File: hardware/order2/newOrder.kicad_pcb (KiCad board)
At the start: 2 copper layers, 200.1 x 330 mm, 683 parts, among them IC1 ATMEGA88-A, IC1 ATMEGA88A-A, J1 RJ45, J1 RJ45_8P8C_8FACH, K1 CONN_3, K1 pow_sel, K2 CONN_3, P1 CONN_4, P1 ISP, P1 UART, P2 CONN_4, P2 Shield, P2 UART, P2 so8, P3 CONN_4, P3 i2c_pow, P4 i2c_chain, P5 12Vin, P6 HOHLBUCHSE, P7 Vccin, P8 ISP, P9 5Vin, SW1 SW1, SW1 SW_RESET, SW2 SCHALTER_2POL, SW3 SW_RESET, U1 LM7805, U1 ST485, U1 TSIC50XF, U2 HYT271, U2 ST485, U3 ST485, U4 ST485, U5 ST485, U6 ST485, U7 ST485, U8 ST485, U9 ST485, X1 20MHz, m3_loch VAL**

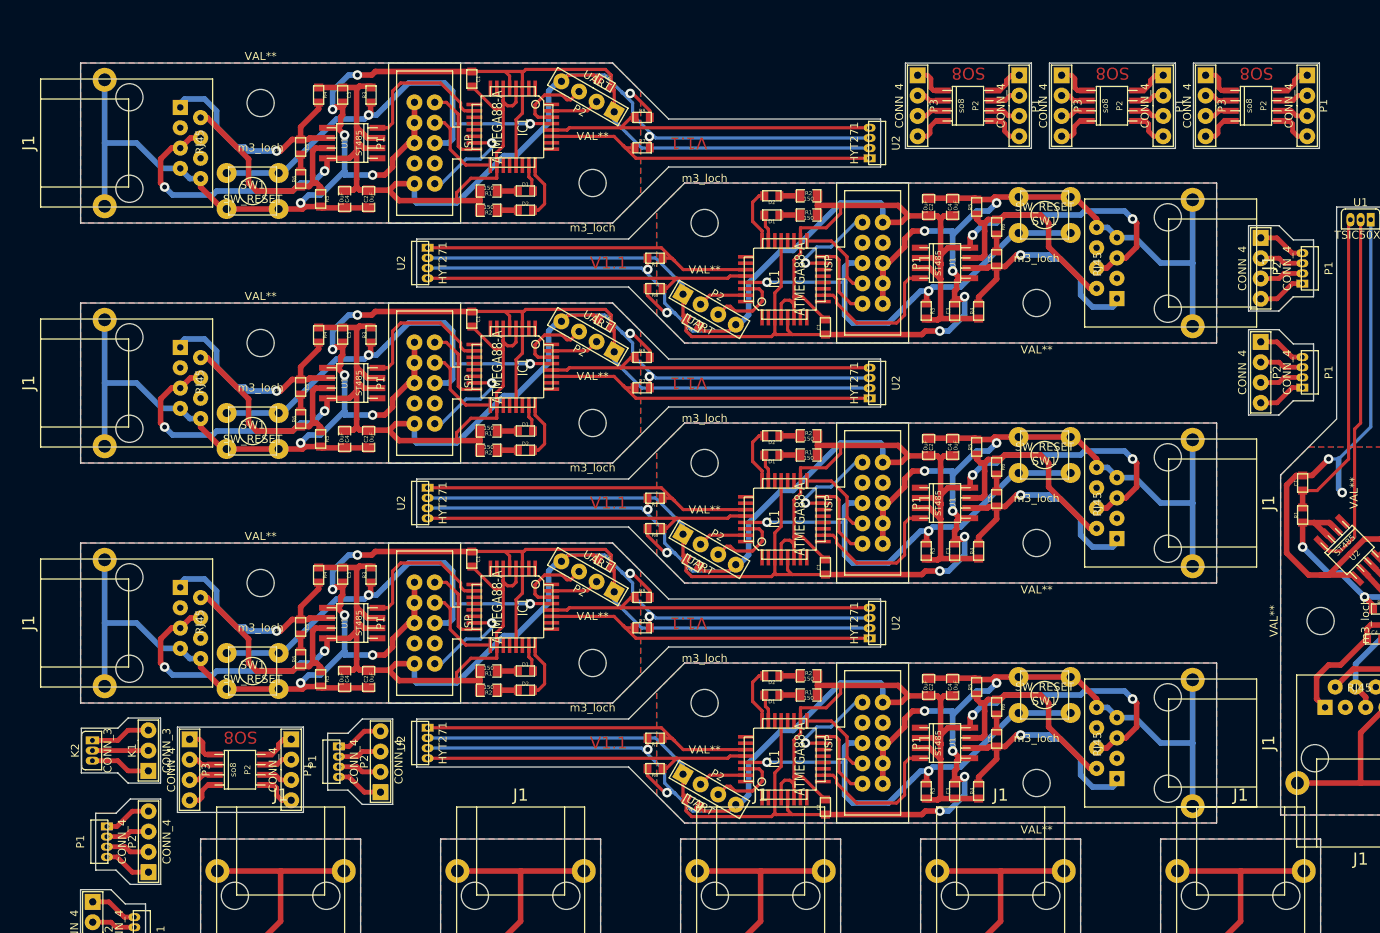
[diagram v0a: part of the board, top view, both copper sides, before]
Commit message: delete humility boards
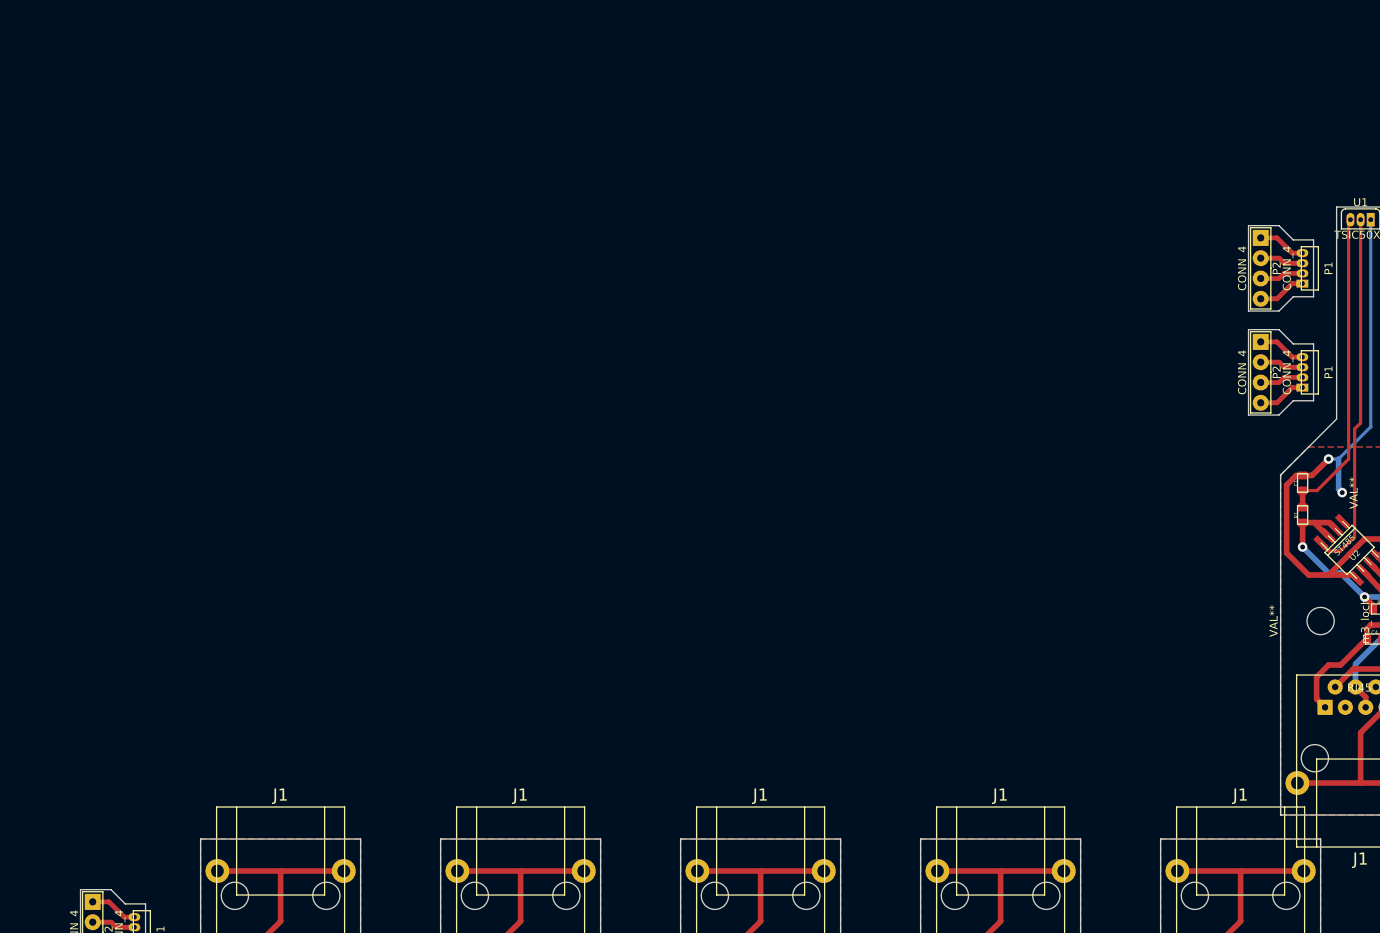
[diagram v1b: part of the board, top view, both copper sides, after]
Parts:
- removed the C1 at (68.9, 82.0)
- removed the C1 at (68.9, 22.0)
- removed the C1 at (113.1, 113.0)
- removed the C1 at (113.1, 53.0)
- removed the C1 at (113.1, 83.0)
- removed the C1 at (68.9, 52.0)
- removed the C2 at (56.0, 97.0)
- removed the C2 at (56.0, 37.0)
- removed the C2 at (126.0, 98.0)
- removed the C2 at (126.0, 38.0)
- removed the C2 at (126.0, 68.0)
- removed the C2 at (56.0, 67.0)
- removed the C3 at (52.8, 84.0)
- removed the C3 at (52.8, 24.0)
- removed the C3 at (129.2, 111.0)
- removed the C3 at (129.2, 51.0)
- removed the C3 at (129.2, 81.0)
- removed the C3 at (52.8, 54.0)
- removed the C4 at (53.0, 97.0)
- removed the C4 at (53.0, 37.0)
- removed the C4 at (129.0, 98.0)
- removed the C4 at (129.0, 38.0)
- removed the C4 at (129.0, 68.0)
- removed the C4 at (53.0, 67.0)
- removed the C5 at (47.5, 90.5)
- removed the C5 at (47.5, 30.5)
- removed the C5 at (134.5, 44.5)
- removed the C5 at (134.5, 74.5)
- removed the C5 at (47.5, 60.5)
- removed the C5 at (134.5, 104.5)
- removed the C6 at (85.5, 82.5)
- removed the C6 at (85.5, 22.5)
- removed the C6 at (96.5, 52.5)
- removed the C6 at (96.5, 82.5)
- removed the C6 at (85.5, 52.5)
- removed the C6 at (96.5, 112.5)
- removed the D1 at (75.6, 96.0)
- removed the D1 at (75.6, 36.0)
- removed the D1 at (106.4, 39.0)
- removed the D1 at (106.4, 69.0)
- removed the D1 at (75.6, 66.0)
- removed the D1 at (106.4, 99.0)
- removed the D2 at (75.6, 98.4)
- removed the D2 at (75.6, 38.4)
- removed the D2 at (106.4, 36.6)
- removed the D2 at (106.4, 66.6)
- removed the D2 at (75.6, 68.4)
- removed the D2 at (106.4, 96.6)
- removed the IC1 at (74.0, 88.0)
- removed the IC1 at (74.0, 28.0)
- removed the IC1 at (108.0, 47.0)
- removed the IC1 at (108.0, 77.0)
- removed the IC1 at (74.0, 58.0)
- removed the IC1 at (108.0, 107.0)
- removed the J1 at (35.0, 90.0)
- removed the J1 at (35.0, 30.0)
- removed the J1 at (147.0, 105.0)
- removed the J1 at (147.0, 45.0)
- removed the J1 at (147.0, 75.0)
- removed the J1 at (35.0, 60.0)
- removed the K1 at (28.5, 105.9)
- removed K2: CONN_3, Tsic_TO92
- removed the P1 at (63.0, 90.0)
- removed the P1 at (63.0, 30.0)
- removed the P1 at (119.0, 45.0)
- removed the P1 at (119.0, 75.0)
- removed the P1 at (63.0, 60.0)
- removed the P1 at (173.3, 25.3)
- removed the P1 at (23.4, 117.3)
- removed the P1 at (119.0, 105.0)
- removed the P1 at (155.3, 25.3)
- removed the P1 at (137.3, 25.3)
- removed the P1 at (46.3, 108.3)
- removed the P1 at (52.4, 107.3)
- removed the P2 at (83.4, 84.2)
- removed the P2 at (83.4, 24.2)
- removed the P2 at (98.6, 50.8)
- removed the P2 at (98.6, 80.8)
- removed the P2 at (83.4, 54.2)
- removed the P2 at (168.9, 25.3)
- removed the P2 at (28.5, 117.3)
- removed the P2 at (98.6, 110.8)
- removed the P2 at (150.9, 25.3)
- removed the P2 at (132.9, 25.3)
- removed the P2 at (41.9, 108.3)
- removed the P2 at (57.5, 107.3)
- removed the P3 at (142.6, 25.3)
- removed the P3 at (124.6, 25.3)
- removed the P3 at (33.6, 108.3)
- removed the P3 at (160.6, 25.3)
- removed the R1 at (71.0, 96.0)
- removed the R1 at (71.0, 36.0)
- removed the R1 at (111.0, 99.0)
- removed the R1 at (111.0, 39.0)
- removed the R1 at (111.0, 69.0)
- removed the R1 at (71.0, 66.0)
- removed the R2 at (71.0, 98.4)
- removed the R2 at (71.0, 38.4)
- removed the R2 at (111.0, 96.6)
- removed the R2 at (111.0, 36.6)
- removed the R2 at (111.0, 66.6)
- removed the R2 at (71.0, 68.4)
- removed the R3 at (56.3, 84.0)
- removed the R3 at (56.3, 24.0)
- removed the R3 at (125.7, 111.0)
- removed the R3 at (125.7, 51.0)
- removed the R3 at (125.7, 81.0)
- removed the R3 at (56.3, 54.0)
- removed the R4 at (49.8, 84.0)
- removed the R4 at (49.8, 24.0)
- removed the R4 at (132.2, 111.0)
- removed the R4 at (132.2, 51.0)
- removed the R4 at (132.2, 81.0)
- removed the R4 at (49.8, 54.0)
- removed the R5 at (50.0, 97.0)
- removed the R5 at (50.0, 37.0)
- removed the R5 at (132.0, 38.0)
- removed the R5 at (132.0, 68.0)
- removed the R5 at (50.0, 67.0)
- removed the R5 at (132.0, 98.0)
- removed the R6 at (47.5, 94.5)
- removed the R6 at (47.5, 34.5)
- removed the R6 at (134.5, 40.5)
- removed the R6 at (134.5, 70.5)
- removed the R6 at (47.5, 64.5)
- removed the R6 at (134.5, 100.5)
- removed the R7 at (90.2, 90.6)
- removed the R7 at (90.2, 30.6)
- removed the R7 at (91.8, 44.4)
- removed the R7 at (91.8, 74.4)
- removed the R7 at (90.2, 60.6)
- removed the R7 at (91.8, 104.4)
- removed the R8 at (90.2, 86.8)
- removed the R8 at (90.2, 26.8)
- removed the R8 at (91.8, 48.2)
- removed the R8 at (91.8, 78.2)
- removed the R8 at (90.2, 56.8)
- removed the R8 at (91.8, 108.2)
- removed the SW1 at (41.5, 96.0)
- removed the SW1 at (41.5, 36.0)
- removed the SW1 at (140.5, 39.0)
- removed the SW1 at (140.5, 69.0)
- removed the SW1 at (41.5, 66.0)
- removed the SW1 at (140.5, 99.0)
- removed the U1 at (52.0, 90.0)
- removed the U1 at (52.0, 30.0)
- removed the U1 at (130.0, 105.0)
- removed the U1 at (130.0, 45.0)
- removed the U1 at (130.0, 75.0)
- removed the U1 at (52.0, 60.0)
- removed the U2 at (118.5, 90.0)
- removed the U2 at (118.5, 30.0)
- removed the U2 at (63.5, 105.0)
- removed the U2 at (63.5, 45.0)
- removed the U2 at (63.5, 75.0)
- removed the U2 at (118.5, 60.0)
- removed the m3_loch at (84.0, 95.0)
- removed the m3_loch at (84.0, 65.0)
- removed the m3_loch at (42.5, 85.0)
- removed the m3_loch at (84.0, 35.0)
- removed the m3_loch at (42.5, 25.0)
- removed the m3_loch at (139.5, 110.0)
- removed the m3_loch at (98.0, 100.0)
- removed the m3_loch at (98.0, 40.0)
- removed the m3_loch at (139.5, 50.0)
- removed the m3_loch at (139.5, 80.0)
- removed the m3_loch at (98.0, 70.0)
- removed the m3_loch at (42.5, 55.0)
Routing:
- net VCC: track 3787.2 -> 2592.3 mm, vias 81 -> 57
- net GND: track 5785.4 -> 4679.1 mm, vias 71 -> 41
- net /RESET: track 655.4 -> 320.7 mm, vias 18 -> 6
- net /SDA: track 498.6 -> 243.5 mm
- net /SCL: track 520.7 -> 267.5 mm
- net /za: track 560.8 -> 385.9 mm, vias 6 -> 0
- net /zb: track 565.0 -> 398.9 mm
- net /DI: track 111.1 -> 0.00 mm
- net /MOSI: track 219.5 -> 148.9 mm, vias 12 -> 6
- net /SCK: track 99.6 -> 35.7 mm
- net /RX: track 199.5 -> 139.1 mm
- net /MISO: track 84.6 -> 26.2 mm
- net N-000002: track 78.2 -> 27.4 mm
- net /LED2: track 96.1 -> 53.3 mm
- net /TX: track 182.5 -> 145.6 mm
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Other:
- outline, holes or cut-outs redrawn
- board text removed: "SO8"
- board text removed: "V1.1"

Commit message: 3 humidity but 19 temperature
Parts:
- added C1: 100nF, SM0603_big, F.Cu at (61.5, 97.8)
- added C1: 100nF, SM0603_big, F.Cu at (440.5, 209.8)
- added C1: 100nF, SM0603_big, F.Cu at (498.1, 363.0)
- added C1: 100nF, SM0603_big, F.Cu at (61.5, 67.8)
- added C1: 100nF, SM0603_big, F.Cu at (388.5, 66.8)
- added C1: 100nF, SM0603_big, F.Cu at (72.5, 97.2)
- added C1: 100nF, SM0603_big, F.Cu at (113.1, 68.0)
- added C1: 100nF, SM0603_big, F.Cu at (399.5, 96.2)
- added C1: 100nF, SM0603_big, F.Cu at (364.5, 370.2)
- added C1: 100nF, SM0603_big, F.Cu at (113.1, 38.0)
- added C1: 100nF, SM0603_big, F.Cu at (68.9, 37.0)
- added C2: 100nF, SM0603_big, F.Cu at (52.8, 112.2)
- added C2: 100nF, SM0603_big, F.Cu at (431.8, 224.2)
- added C2: 10uF, SM0805_big, F.Cu at (511.0, 348.0)
- added C2: 100nF, SM0603_big, F.Cu at (52.8, 82.2)
- added C2: 100nF, SM0603_big, F.Cu at (379.8, 81.2)
- added C2: 100nF, SM0603_big, F.Cu at (81.2, 82.8)
- added C2: 10uF, SM0805_big, F.Cu at (126.0, 53.0)
- added C2: 100nF, SM0603_big, F.Cu at (408.2, 81.8)
- added C2: 100nF, SM0603_big, F.Cu at (373.2, 355.8)
- added C2: 10uF, SM0805_big, F.Cu at (126.0, 23.0)
- added C2: 10uF, SM0805_big, F.Cu at (56.0, 52.0)
- added C3: 10uF, SM0805_big, F.Cu at (49.2, 112.2)
- added C3: 10uF, SM0805_big, F.Cu at (428.2, 224.2)
- added C3: 100nF, SM0603_big, F.Cu at (514.2, 361.0)
- added C3: 10uF, SM0805_big, F.Cu at (49.2, 82.2)
- added C3: 10uF, SM0805_big, F.Cu at (376.2, 81.2)
- added C3: 10uF, SM0805_big, F.Cu at (84.8, 82.8)
- added C3: 100nF, SM0603_big, F.Cu at (129.2, 66.0)
- added C3: 10uF, SM0805_big, F.Cu at (411.8, 81.8)
- added C3: 10uF, SM0805_big, F.Cu at (376.8, 355.8)
- added C3: 100nF, SM0603_big, F.Cu at (129.2, 36.0)
- added C3: 100nF, SM0603_big, F.Cu at (52.8, 39.0)
- added C4: 100nF, SM0603_big, F.Cu at (42.0, 106.8)
- added C4: 100nF, SM0603_big, F.Cu at (421.0, 218.8)
- added C4: 10uF, SM0805_big, F.Cu at (514.0, 348.0)
- added C4: 100nF, SM0603_big, F.Cu at (42.0, 76.8)
- added C4: 100nF, SM0603_big, F.Cu at (369.0, 75.8)
- added C4: 100nF, SM0603_big, F.Cu at (92.0, 88.2)
- added C4: 10uF, SM0805_big, F.Cu at (129.0, 53.0)
- added C4: 100nF, SM0603_big, F.Cu at (419.0, 87.2)
- added C4: 100nF, SM0603_big, F.Cu at (384.0, 361.2)
- added C4: 10uF, SM0805_big, F.Cu at (129.0, 23.0)
- added C4: 10uF, SM0805_big, F.Cu at (53.0, 52.0)
- added C5: 100nF, SM0603_big, F.Cu at (134.5, 59.5)
- added C5: 100nF, SM0603_big, F.Cu at (134.5, 29.5)
- added C5: 100nF, SM0603_big, F.Cu at (47.5, 45.5)
- added C5: 100nF, SM0603_big, F.Cu at (519.5, 354.5)
- added C6: 100nF, SM0603_big, F.Cu at (96.5, 67.5)
- added C6: 100nF, SM0603_big, F.Cu at (96.5, 37.5)
- added C6: 100nF, SM0603_big, F.Cu at (85.5, 37.5)
- added C6: 100nF, SM0603_big, F.Cu at (481.5, 362.5)
- added D1: LED, SM0603_big, F.Cu at (106.4, 54.0)
- added D1: LED, SM0603_big, F.Cu at (106.4, 24.0)
- added D1: LED, SM0603_big, F.Cu at (75.6, 51.0)
- added D1: LED, SM0603_big, F.Cu at (491.4, 349.0)
- added D2: LED, SM0603_big, F.Cu at (106.4, 51.6)
- added D2: LED, SM0603_big, F.Cu at (106.4, 21.6)
- added D2: LED, SM0603_big, F.Cu at (75.6, 53.4)
- added D2: LED, SM0603_big, F.Cu at (491.4, 346.6)
- added IC1: ATMEGA88-A, TQFP32, F.Cu at (108.0, 62.0)
- added IC1: ATMEGA88-A, TQFP32, F.Cu at (108.0, 32.0)
- added IC1: ATMEGA88-A, TQFP32, F.Cu at (74.0, 43.0)
- added IC1: ATMEGA88-A, TQFP32, F.Cu at (493.0, 357.0)
- added J1: RJ45, RJ45_8P8_simple, F.Cu at (36.0, 105.0)
- added J1: RJ45, RJ45_8P8_simple, F.Cu at (415.0, 217.0)
- added J1: RJ45, RJ45_8P8_simple, F.Cu at (532.0, 355.0)
- added J1: RJ45, RJ45_8P8_simple, F.Cu at (36.0, 75.0)
- added J1: RJ45, RJ45_8P8_simple, F.Cu at (363.0, 74.0)
- added J1: RJ45, RJ45_8P8_simple, F.Cu at (98.0, 90.0)
- added J1: RJ45, RJ45_8P8_simple, F.Cu at (147.0, 60.0)
- added J1: RJ45, RJ45_8P8_simple, F.Cu at (425.0, 89.0)
- added J1: RJ45, RJ45_8P8_simple, F.Cu at (390.0, 363.0)
- added J1: RJ45, RJ45_8P8_simple, F.Cu at (147.0, 30.0)
- added J1: RJ45, RJ45_8P8_simple, F.Cu at (35.0, 45.0)
- added P1: ISP, wannenstecker_2x5_rm254, F.Cu at (119.0, 60.0)
- added P1: ISP, wannenstecker_2x5_rm254, F.Cu at (504.0, 355.0)
- added P1: ISP, wannenstecker_2x5_rm254, F.Cu at (119.0, 30.0)
- added P1: ISP, wannenstecker_2x5_rm254, F.Cu at (63.0, 45.0)
- added P2: UART, Stiftleiste_4x1, F.Cu at (98.6, 65.8)
- added P2: UART, Stiftleiste_4x1, F.Cu at (483.6, 360.8)
- added P2: UART, Stiftleiste_4x1, F.Cu at (98.6, 35.8)
- added P2: UART, Stiftleiste_4x1, F.Cu at (83.4, 39.2)
- added R1: 220, SM0603_big, F.Cu at (57.5, 97.8)
- added R1: 220, SM0603_big, F.Cu at (436.5, 209.8)
- added R1: 150, SM0805_big, F.Cu at (496.0, 349.0)
- added R1: 220, SM0603_big, F.Cu at (57.5, 67.8)
- added R1: 220, SM0603_big, F.Cu at (384.5, 66.8)
- added R1: 220, SM0603_big, F.Cu at (76.5, 97.2)
- added R1: 150, SM0805_big, F.Cu at (111.0, 54.0)
- added R1: 220, SM0603_big, F.Cu at (403.5, 96.2)
- added R1: 220, SM0603_big, F.Cu at (368.5, 370.2)
- added R1: 150, SM0805_big, F.Cu at (111.0, 24.0)
- added R1: 150, SM0805_big, F.Cu at (71.0, 51.0)
- added R2: 22k, SM0603_big, F.Cu at (45.8, 107.5)
- added R2: 22k, SM0603_big, F.Cu at (424.8, 219.5)
- added R2: 150, SM0805_big, F.Cu at (496.0, 346.6)
- added R2: 22k, SM0603_big, F.Cu at (45.8, 77.5)
- added R2: 22k, SM0603_big, F.Cu at (372.8, 76.5)
- added R2: 22k, SM0603_big, F.Cu at (88.2, 87.5)
- added R2: 150, SM0805_big, F.Cu at (111.0, 51.6)
- added R2: 22k, SM0603_big, F.Cu at (415.2, 86.5)
- added R2: 22k, SM0603_big, F.Cu at (380.2, 360.5)
- added R2: 150, SM0805_big, F.Cu at (111.0, 21.6)
- added R2: 150, SM0805_big, F.Cu at (71.0, 53.4)
- added R3: 22k, SM0603_big, F.Cu at (45.8, 112.5)
- added R3: 22k, SM0603_big, F.Cu at (424.8, 224.5)
- added R3: 10k, SM0603_big, F.Cu at (510.7, 361.0)
- added R3: 22k, SM0603_big, F.Cu at (45.8, 82.5)
- added R3: 22k, SM0603_big, F.Cu at (372.8, 81.5)
- added R3: 22k, SM0603_big, F.Cu at (88.2, 82.5)
- added R3: 10k, SM0603_big, F.Cu at (125.7, 66.0)
- added R3: 22k, SM0603_big, F.Cu at (415.2, 81.5)
- added R3: 22k, SM0603_big, F.Cu at (380.2, 355.5)
- added R3: 10k, SM0603_big, F.Cu at (125.7, 36.0)
- added R3: 10k, SM0603_big, F.Cu at (56.3, 39.0)
- added R4: 120, SM0603_big, F.Cu at (42.0, 110.8)
- added R4: 120, SM0603_big, F.Cu at (421.0, 222.8)
- added R4: 22k, SM0603_big, F.Cu at (517.2, 361.0)
- added R4: 120, SM0603_big, F.Cu at (42.0, 80.8)
- added R4: 120, SM0603_big, F.Cu at (369.0, 79.8)
- added R4: 120, SM0603_big, F.Cu at (92.0, 84.2)
- added R4: 22k, SM0603_big, F.Cu at (132.2, 66.0)
- added R4: 120, SM0603_big, F.Cu at (419.0, 83.2)
- added R4: 120, SM0603_big, F.Cu at (384.0, 357.2)
- added R4: 22k, SM0603_big, F.Cu at (132.2, 36.0)
- added R4: 22k, SM0603_big, F.Cu at (49.8, 39.0)
- added R5: 22k, SM0603_big, F.Cu at (132.0, 53.0)
- added R5: 22k, SM0603_big, F.Cu at (132.0, 23.0)
- added R5: 22k, SM0603_big, F.Cu at (50.0, 52.0)
- added R5: 22k, SM0603_big, F.Cu at (517.0, 348.0)
- added R6: 120, SM0603_big, F.Cu at (134.5, 55.5)
- added R6: 120, SM0603_big, F.Cu at (134.5, 25.5)
- added R6: 120, SM0603_big, F.Cu at (47.5, 49.5)
- added R6: 120, SM0603_big, F.Cu at (519.5, 350.5)
- added R7: 2k2, SM0603_big, F.Cu at (91.8, 59.4)
- added R7: 2k2, SM0603_big, F.Cu at (91.8, 29.4)
- added R7: 2k2, SM0603_big, F.Cu at (90.2, 45.6)
- added R7: 2k2, SM0603_big, F.Cu at (476.8, 354.4)
- added R8: 2k2, SM0603_big, F.Cu at (91.8, 63.2)
- added R8: 2k2, SM0603_big, F.Cu at (91.8, 33.2)
- added R8: 2k2, SM0603_big, F.Cu at (90.2, 41.8)
- added R8: 2k2, SM0603_big, F.Cu at (476.8, 358.2)
- added SW1: SW_RESET, Taster_6mm, F.Cu at (140.5, 54.0)
- added SW1: SW_RESET, Taster_6mm, F.Cu at (140.5, 24.0)
- added SW1: SW_RESET, Taster_6mm, F.Cu at (41.5, 51.0)
- added SW1: SW_RESET, Taster_6mm, F.Cu at (525.5, 349.0)
- added U1: TSIC50XF, Tsic_TO92, F.Cu at (92.5, 105.0)
- added U1: TSIC50XF, Tsic_TO92, F.Cu at (471.5, 217.0)
- added U1: ST485, st485, F.Cu at (515.0, 355.0)
- added U1: TSIC50XF, Tsic_TO92, F.Cu at (92.5, 75.0)
- added U1: TSIC50XF, Tsic_TO92, F.Cu at (419.5, 74.0)
- added U1: TSIC50XF, Tsic_TO92, F.Cu at (41.5, 90.0)
- added U1: ST485, st485, F.Cu at (130.0, 60.0)
- added U1: TSIC50XF, Tsic_TO92, F.Cu at (368.5, 89.0)
- added U1: TSIC50XF, Tsic_TO92, F.Cu at (333.5, 363.0)
- added U1: ST485, st485, F.Cu at (130.0, 30.0)
- added U1: ST485, st485, F.Cu at (52.0, 45.0)
- added U2: ST485, st485, F.Cu at (51.8, 105.0)
- added U2: ST485, st485, F.Cu at (430.8, 217.0)
- added U2: HYT271, HYT271, F.Cu at (448.5, 355.0)
- added U2: ST485, st485, F.Cu at (51.8, 75.0)
- added U2: ST485, st485, F.Cu at (378.8, 74.0)
- added U2: ST485, st485, F.Cu at (82.2, 90.0)
- added U2: HYT271, HYT271, F.Cu at (63.5, 60.0)
- added U2: ST485, st485, F.Cu at (409.2, 89.0)
- added U2: ST485, st485, F.Cu at (374.2, 363.0)
- added U2: HYT271, HYT271, F.Cu at (63.5, 30.0)
- added U2: HYT271, HYT271, F.Cu at (118.5, 45.0)
- added m3_loch: VAL**, m3_loch, F.Cu at (60.2, 110.0)
- added m3_loch: VAL**, m3_loch, F.Cu at (139.5, 65.0)
- added m3_loch: VAL**, m3_loch, F.Cu at (416.8, 94.0)
- added m3_loch: VAL**, m3_loch, F.Cu at (400.8, 84.0)
- added m3_loch: VAL**, m3_loch, F.Cu at (365.8, 358.0)
- added m3_loch: VAL**, m3_loch, F.Cu at (381.8, 368.0)
- added m3_loch: VAL**, m3_loch, F.Cu at (98.0, 25.0)
- added m3_loch: VAL**, m3_loch, F.Cu at (139.5, 35.0)
- added m3_loch: VAL**, m3_loch, F.Cu at (84.0, 50.0)
- added m3_loch: VAL**, m3_loch, F.Cu at (42.5, 40.0)
- added m3_loch: VAL**, m3_loch, F.Cu at (44.2, 100.0)
- added m3_loch: VAL**, m3_loch, F.Cu at (423.2, 212.0)
- added m3_loch: VAL**, m3_loch, F.Cu at (439.2, 222.0)
- added m3_loch: VAL**, m3_loch, F.Cu at (60.2, 80.0)
- added m3_loch: VAL**, m3_loch, F.Cu at (44.2, 70.0)
- added m3_loch: VAL**, m3_loch, F.Cu at (524.5, 360.0)
- added m3_loch: VAL**, m3_loch, F.Cu at (483.0, 350.0)
- added m3_loch: VAL**, m3_loch, F.Cu at (371.2, 69.0)
- added m3_loch: VAL**, m3_loch, F.Cu at (387.2, 79.0)
- added m3_loch: VAL**, m3_loch, F.Cu at (73.8, 85.0)
- added m3_loch: VAL**, m3_loch, F.Cu at (89.8, 95.0)
- added m3_loch: VAL**, m3_loch, F.Cu at (98.0, 55.0)
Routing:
- net GND: track 4679.1 -> 6304.5 mm, vias 41 -> 75
- net VCC: track 2592.3 -> 3792.6 mm, vias 57 -> 94
- net N-000007: track 739.7 -> 1058.4 mm
- net /za: track 385.9 -> 671.3 mm, vias 0 -> 4
- net /zb: track 398.9 -> 684.1 mm
- net N-0000010: track 632.0 -> 908.5 mm
- net /RESET: track 320.7 -> 543.9 mm, vias 6 -> 14
- net /SDA: track 243.5 -> 413.6 mm
- net /SCL: track 267.5 -> 436.3 mm
- net /DI: track 0.00 -> 74.1 mm
- net /MOSI: track 148.9 -> 196.0 mm, vias 6 -> 10
- net /SCK: track 35.7 -> 78.3 mm
- net /RX: track 139.1 -> 179.3 mm
- net /MISO: track 26.2 -> 65.1 mm
- net /LED2: track 53.3 -> 81.8 mm
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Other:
- board size 200.1 x 330 mm -> 527 x 353 mm
- rule pad_to_mask_clearance: 0.15 -> 0
- board text added: "v1.1"
